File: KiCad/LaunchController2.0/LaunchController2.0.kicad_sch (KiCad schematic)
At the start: 39 parts, among them J1 CONN_ICSP, J2 CONN_USB, J3 USB_C_Receptacle_USB2.0_16P, U1 ATmega2560-16A, U2 FT232RNL, U3 USBLC6-2SC6, Y1 HUSG-16.000-20

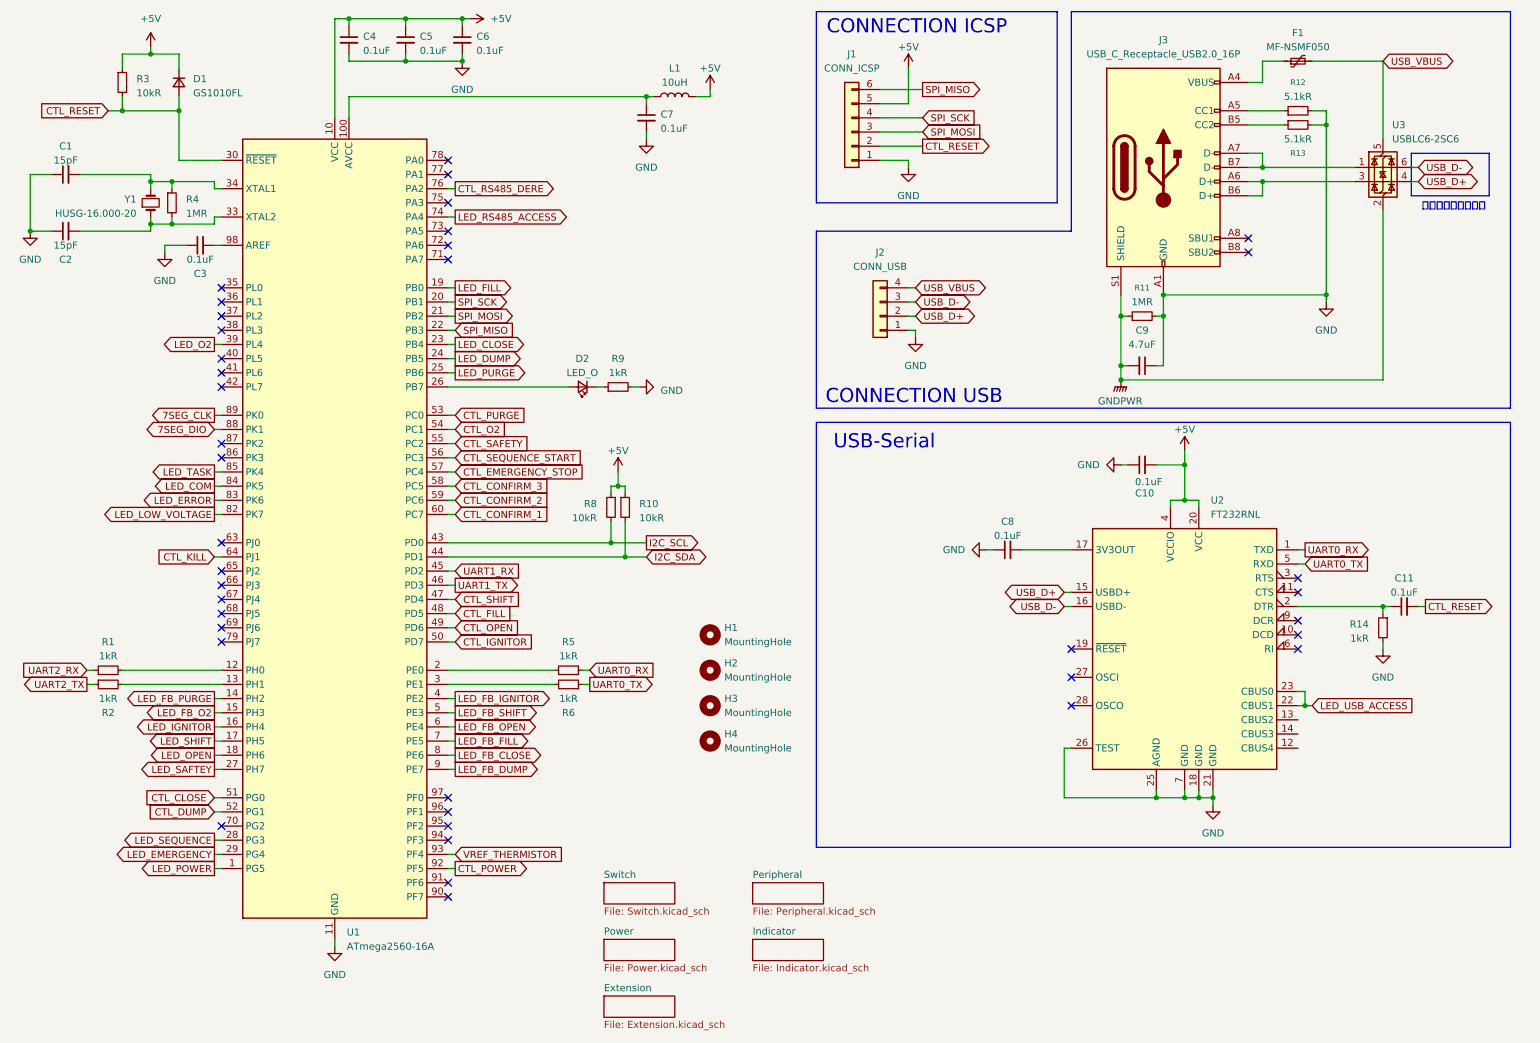
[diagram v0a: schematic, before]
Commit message: シルクなどを調整
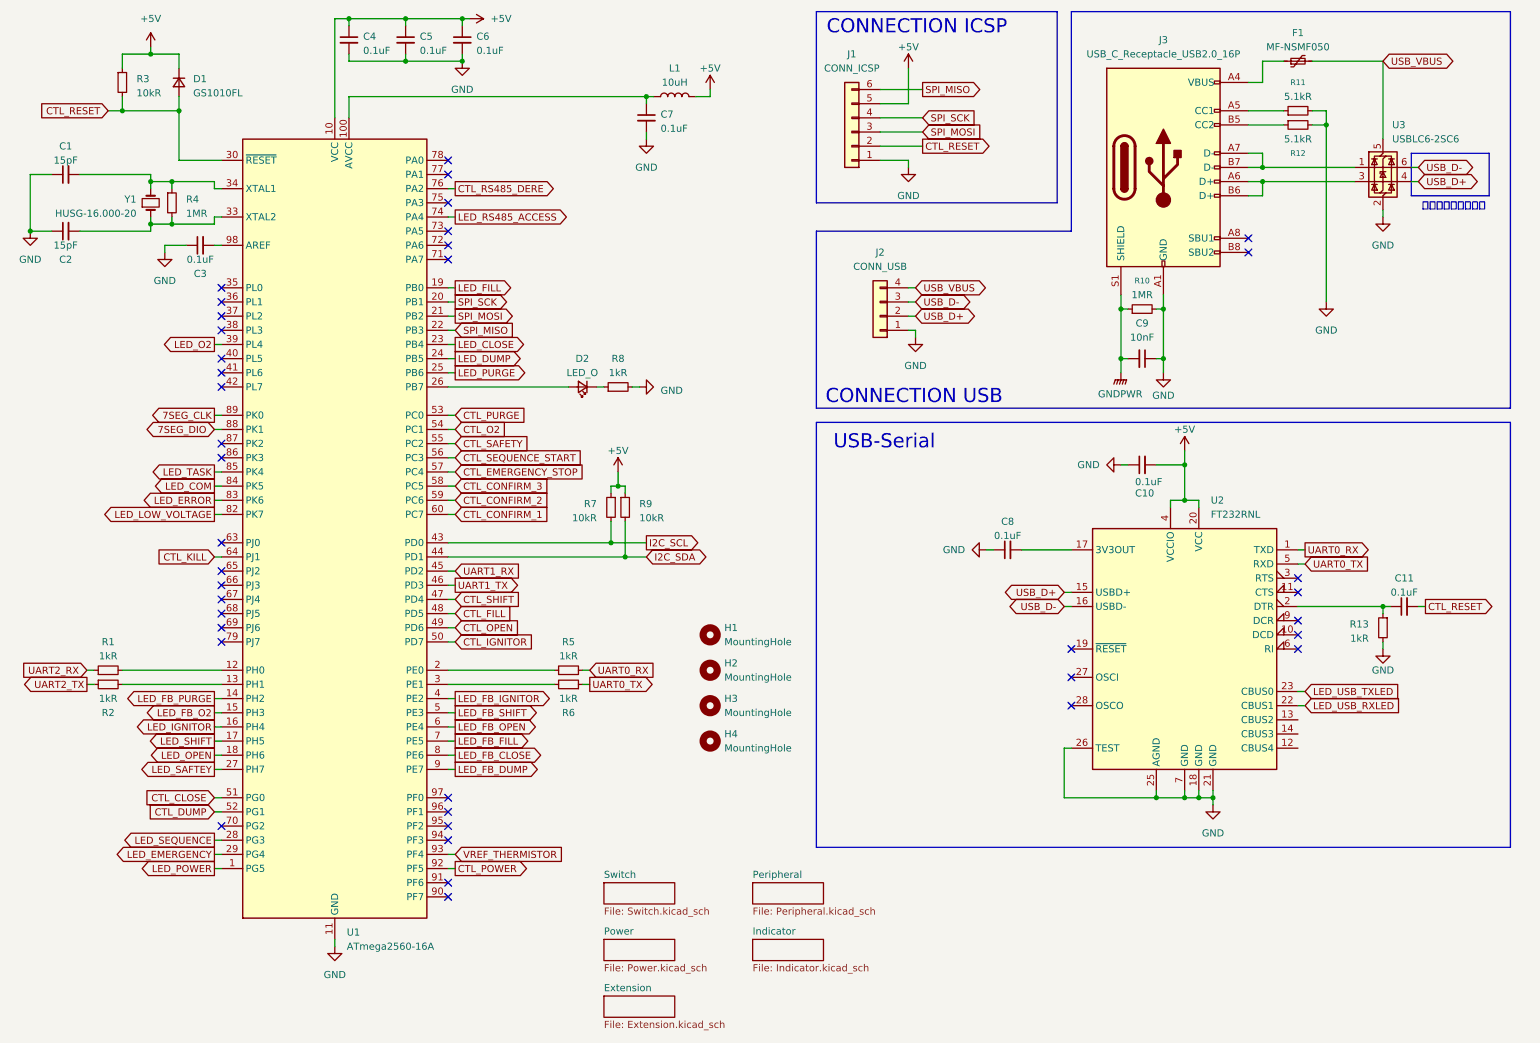
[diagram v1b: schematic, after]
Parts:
- C1, C2: Digikey_PN (none) -> 490-4941-1-ND
- C10, C11, C3, C4, C5, C6, C7, C8: Digikey_PN (none) -> 490-8020-1-ND
- C9: value 4.7uF -> 10nF; footprint Capacitor_SMD:C_0603_1608Metric_Pad1.08x0.95mm_HandSolder -> Capacitor_SMD:C_0805_2012Metric_Pad1.18x1.45mm_HandSolder; Digikey_PN (none) -> 490-GCM21B5C2E103FX0ALCT-ND
- D1: Akiduki_PN (none) -> 106014
- D2: Digikey_PN (none) -> SML-D12D8WT86CCT-ND
- F1: Akiduki_PN (none) -> 115300
- J1: Akiduki_PN (none) -> 101669
- J2: Digikey_PN (none) -> 2946-2601-3104-ND
- J3: Akiduki_PN (none) -> 114356
- L1: Akiduki_PN (none) -> 114977
- R1, R2, R5, R6: Digikey_PN (none) -> 2019-RK73H1JTTD1001FCT-ND
- R10: renamed from R11; footprint Resistor_SMD:R_0603_1608Metric_Pad0.98x0.95mm_HandSolder -> Resistor_SMD:R_1206_3216Metric_Pad1.30x1.75mm_HandSolder; Digikey_PN (none) -> 2019-RK73H2BTTD1004FCT-ND
- R11: renamed from R12; Digikey_PN (none) -> 2019-RK73H1JTTD5101FCT-ND
- R12: renamed from R13; Digikey_PN (none) -> 2019-RK73H1JTTD5101FCT-ND
- R13: renamed from R14; Digikey_PN (none) -> 2019-RK73H1JTTD1001FCT-ND
- R3: Digikey_PN (none) -> 2019-RK73H1JTTD1002FCT-ND
- R4: Digikey_PN (none) -> 2019-RK73H1JTTD1004FCT-ND
- R7: renamed from R8; Digikey_PN (none) -> 2019-RK73H1JTTD1002FCT-ND
- R8: renamed from R9; Digikey_PN (none) -> 2019-RK73H1JTTD1001FCT-ND
- R9: renamed from R10; Digikey_PN (none) -> 2019-RK73H1JTTD1002FCT-ND
- U1: Akiduki_PN (none) -> 116567
- U2: Akiduki_PN (none) -> 118243
- U3: Digikey_PN (none) -> 497-5235-1-ND
- Y1: Akiduki_PN (none) -> 108671
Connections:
- net GND: now also U3.2 (GND)
- net GNDPWR: no longer U3.2 (GND)
- net LED_USB_ACCESS renamed LED_USB_RXLED
- net LED_USB_RXLED: no longer U2.23 (CBUS0)
- new net LED_USB_TXLED: U2.23 (CBUS0)
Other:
- company: (none) -> Tokai Student Rocket Project
- moved on the sheet: C9, R10

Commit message: BOM作成
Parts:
- C1, C2: Akiduki_PN (none) -> 113312; Digikey_PN 490-4941-1-ND -> (none)
- C10, C11, C3, C4, C5, C6, C7, C8: Akiduki_PN (none) -> 114559; Digikey_PN 490-8020-1-ND -> (none)
- D2: Digikey_PN SML-D12D8WT86CCT-ND -> SML-D15DWT86CCT-ND
- H1, H2, H3, H4: footprint MountingHole:MountingHole_4mm -> MountingHole:MountingHole_4.3mm_M4_Pad_Via; now in the parts list
- U3: value USBLC6-2SC6 -> SP0504SHTG; Digikey_PN 497-5235-1-ND -> F5775CT-ND
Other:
- note added: "配線（符号）に気をつけよう"
- note removed: "向きに気をつけよう"
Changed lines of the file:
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@@
 		)
 	)
-	(text "向きに気をつけよう"
+	(text "配線（符号）に気をつけよう"
 		(exclude_from_sim no)
 		(at 270.51 49.022 0)
@@
 			)
 		)
-		(property "Datasheet" "https://www.digikey.jp/short/bbj307jp"
+		(property "Datasheet" "https://akizukidenshi.com/catalog/g/g113312/"
 			(at 21.59 53.34 0)
 			(effects
@@
 			)
 		)
-		(property "Digikey_PN" "490-4941-1-ND"
+		(property "Digikey_PN" ""
+			(at 21.59 53.34 90)
+			(effects
+				(font
+					(size 1.27 1.27)
+				)
+				(hide yes)
+			)
+		)
+		(property "Akiduki_PN" "113312"
 			(at 21.59 53.34 90)
 			(effects
@@
 			)
 		)
-		(property "Datasheet" "https://www.digikey.jp/short/ftvh328f"
+		(property "Datasheet" "https://akizukidenshi.com/catalog/g/g114559/"
 			(at 72.39 19.05 0)
 			(effects
@@
 			)
 		)
-		(property "Digikey_PN" "490-8020-1-ND"
+		(property "Digikey_PN" ""
+			(at 72.39 19.05 0)
+			(effects
+				(font
+					(size 1.27 1.27)
+				)
+				(hide yes)
+			)
+		)
+		(property "Akiduki_PN" "114559"
 			(at 72.39 19.05 0)
 			(effects
@@
 			)
 		)
-		(property "Datasheet" "https://www.digikey.jp/short/ftvh328f"
+		(property "Datasheet" "https://akizukidenshi.com/catalog/g/g114559/"
 			(at 190.5 110.49 0)
 			(effects
@@
 			)
 		)
-		(property "Digikey_PN" "490-8020-1-ND"
+		(property "Digikey_PN" ""
+			(at 190.5 110.49 90)
+			(effects
+				(font
+					(size 1.27 1.27)
+				)
+				(hide yes)
+			)
+		)
+		(property "Akiduki_PN" "114559"
 			(at 190.5 110.49 90)
 			(effects
@@
 			)
 		)
-		(property "Datasheet" "https://www.digikey.jp/short/ftvh328f"
+		(property "Datasheet" "https://akizukidenshi.com/catalog/g/g114559/"
 			(at 82.55 19.05 0)
 			(effects
@@
 			)
 		)
-		(property "Digikey_PN" "490-8020-1-ND"
+		(property "Digikey_PN" ""
+			(at 82.55 19.05 0)
+			(effects
+				(font
+					(size 1.27 1.27)
+				)
+				(hide yes)
+			)
+		)
+		(property "Akiduki_PN" "114559"
 			(at 82.55 19.05 0)
 			(effects
@@
 			)
 		)
+		(property "Mouser_PN" ""
+			(at 214.63 76.2 0)
+			(effects
+				(font
+					(size 1.27 1.27)
+				)
+				(hide yes)
+			)
+		)
+		(property "Akiduki_PN" ""
+			(at 214.63 76.2 0)
+			(effects
+				(font
+					(size 1.27 1.27)
+				)
+				(hide yes)
+			)
+		)
 		(pin "1"
 		)
@@
 			)
 		)
-		(property "Datasheet" "https://www.digikey.jp/short/ftvh328f"
+		(property "Datasheet" "https://akizukidenshi.com/catalog/g/g114559/"
 			(at 45.72 55.88 0)
 			(effects
@@
 			)
 		)
-		(property "Digikey_PN" "490-8020-1-ND"
+		(property "Digikey_PN" ""
+			(at 45.72 55.88 90)
+			(effects
+				(font
+					(size 1.27 1.27)
+				)
+				(hide yes)
+			)
+		)
+		(property "Akiduki_PN" "114559"
 			(at 45.72 55.88 90)
 			(effects
@@
 		(unit 1)
 		(exclude_from_sim no)
-		(in_bom no)
+		(in_bom yes)
 		(on_board yes)
 		(dnp no)
@@
 			)
 		)
-		(property "Footprint" "MountingHole:MountingHole_4mm"
+		(property "Footprint" "MountingHole:MountingHole_4.3mm_M4_Pad_Via"
 			(at 137.16 125.73 0)
 			(effects
@@
 			)
 		)
+		(property "Digikey_PN" ""
+			(at 137.16 125.73 0)
+			(effects
+				(font
+					(size 1.27 1.27)
+				)
+				(hide yes)
+			)
+		)
+		(property "Mouser_PN" ""
+			(at 137.16 125.73 0)
+			(effects
+				(font
+					(size 1.27 1.27)
+				)
+				(hide yes)
+			)
+		)
+		(property "Akiduki_PN" ""
+			(at 137.16 125.73 0)
+			(effects
+				(font
+					(size 1.27 1.27)
+				)
+				(hide yes)
+			)
+		)
 		(instances
 			(project ""
@@
 			)
 		)
-		(property "Value" "USBLC6-2SC6"
+		(property "Value" "SP0504SHTG"
 			(at 259.4611 36.83 0)
 			(effects
@@
 			)
 		)
-		(property "Datasheet" "https://www.digikey.jp/short/rv3q24zz"
+		(property "Datasheet" "https://www.digikey.jp/short/npv4wv57"
 			(at 259.08 50.165 0)
 			(effects
@@
 			)
 		)
-		(property "Digikey_PN" "497-5235-1-ND"
+		(property "Digikey_PN" "F5775CT-ND"
 			(at 257.81 41.91 0)
 			(effects
@@
 			)
 		)
-		(property "Datasheet" "https://www.digikey.jp/short/ftvh328f"
+		(property "Datasheet" "https://akizukidenshi.com/catalog/g/g114559/"
 			(at 261.62 120.65 0)
 			(effects
@@
 			)
 		)
-		(property "Digikey_PN" "490-8020-1-ND"
+		(property "Digikey_PN" ""
+			(at 261.62 120.65 90)
+			(effects
+				(font
+					(size 1.27 1.27)
+				)
+				(hide yes)
+			)
+		)
+		(property "Akiduki_PN" "114559"
 			(at 261.62 120.65 90)
 			(effects
@@
 			)
 		)
-		(property "Datasheet" "https://www.digikey.jp/short/ftvh328f"
+		(property "Datasheet" "https://akizukidenshi.com/catalog/g/g114559/"
 			(at 214.63 95.25 0)
 			(effects
@@
 			)
 		)
-		(property "Digikey_PN" "490-8020-1-ND"
+		(property "Digikey_PN" ""
+			(at 214.63 95.25 90)
+			(effects
+				(font
+					(size 1.27 1.27)
+				)
+				(hide yes)
+			)
+		)
+		(property "Akiduki_PN" "114559"
 			(at 214.63 95.25 90)
 			(effects
@@
 		(unit 1)
 		(exclude_from_sim no)
-		(in_bom no)
+		(in_bom yes)
 		(on_board yes)
 		(dnp no)
@@
 			)
 		)
-		(property "Footprint" "MountingHole:MountingHole_4mm"
+		(property "Footprint" "MountingHole:MountingHole_4.3mm_M4_Pad_Via"
 			(at 137.16 132.08 0)
 			(effects
@@
 			)
 		)
-		(property "Datasheet" "https://www.digikey.jp/short/ftvh328f"
+		(property "Datasheet" "https://akizukidenshi.com/catalog/g/g114559/"
 			(at 125.73 33.02 0)
 			(effects
@@
 			)
 		)
-		(property "Digikey_PN" "490-8020-1-ND"
+		(property "Digikey_PN" ""
+			(at 125.73 33.02 0)
+			(effects
+				(font
+					(size 1.27 1.27)
+				)
+				(hide yes)
+			)
+		)
+		(property "Akiduki_PN" "114559"
 			(at 125.73 33.02 0)
 			(effects
@@
 		(unit 1)
 		(exclude_from_sim no)
-		(in_bom no)
+		(in_bom yes)
 		(on_board yes)
 		(dnp no)
@@
 			)
 		)
-		(property "Footprint" "MountingHole:MountingHole_4mm"
+		(property "Footprint" "MountingHole:MountingHole_4.3mm_M4_Pad_Via"
 			(at 137.16 138.43 0)
 			(effects
@@
 			)
 		)
+		(property "Digikey_PN" ""
+			(at 218.44 41.91 0)
+			(effects
+				(font
+					(size 1.27 1.27)
+				)
+				(hide yes)
+			)
+		)
+		(property "Mouser_PN" ""
+			(at 218.44 41.91 0)
+			(effects
+				(font
+					(size 1.27 1.27)
+				)
+				(hide yes)
+			)
+		)
 		(pin "A1"
 		)
@@
 			)
 		)
-		(property "Datasheet" "https://www.digikey.jp/short/ftvh328f"
+		(property "Datasheet" "https://akizukidenshi.com/catalog/g/g114559/"
 			(at 92.71 19.05 0)
 			(effects
@@
 			)
 		)
-		(property "Digikey_PN" "490-8020-1-ND"
+		(property "Digikey_PN" ""
+			(at 92.71 19.05 0)
+			(effects
+				(font
+					(size 1.27 1.27)
+				)
+				(hide yes)
+			)
+		)
+		(property "Akiduki_PN" "114559"
 			(at 92.71 19.05 0)
 			(effects
@@
 		(unit 1)
 		(exclude_from_sim no)
-		(in_bom no)
+		(in_bom yes)
 		(on_board yes)
 		(dnp no)
@@
 			)
 		)
-		(property "Footprint" "MountingHole:MountingHole_4mm"
+		(property "Footprint" "MountingHole:MountingHole_4.3mm_M4_Pad_Via"
 			(at 137.16 144.78 0)
 			(effects
@@
 			)
 		)
-		(property "Datasheet" "https://www.digikey.jp/short/3p7j3w3t"
+		(property "Datasheet" "https://www.digikey.jp/short/3ww5zf50"
 			(at 114.3 81.28 90)
 			(effects
@@
 			)
 		)
-		(property "Digikey_PN" "SML-D12D8WT86CCT-ND"
+		(property "Digikey_PN" "SML-D15DWT86CCT-ND"
 			(at 114.3 81.28 0)
 			(effects
@@
 			)
 		)
-		(property "Datasheet" "https://www.digikey.jp/short/bbj307jp"
+		(property "Datasheet" "https://akizukidenshi.com/catalog/g/g113312/"
 			(at 21.59 43.18 0)
 			(effects
@@
 			)
 		)
-		(property "Digikey_PN" "490-4941-1-ND"
+		(property "Digikey_PN" ""
+			(at 21.59 43.18 90)
+			(effects
+				(font
+					(size 1.27 1.27)
+				)
+				(hide yes)
+			)
+		)
+		(property "Akiduki_PN" "113312"
 			(at 21.59 43.18 90)
 			(effects

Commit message: とりあえずプッシュ
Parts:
- C9: DigiKey_PN (none) -> 490-GCM21B5C2E103FX0ALCT-ND
- D2: DigiKey_PN (none) -> 160-1434-1-ND
- J2: DigiKey_PN (none) -> 2946-2601-3104-ND
- R1, R13, R2, R5, R6, R8: DigiKey_PN (none) -> 2019-RK73H1JTTD1001FCT-ND
- R10: DigiKey_PN (none) -> 2019-RK73H2BTTD1004FCT-ND
- R11, R12: DigiKey_PN (none) -> 2019-RK73H1JTTD5101FCT-ND
- R3, R7, R9: DigiKey_PN (none) -> 2019-RK73H1JTTD1002FCT-ND
- R4: DigiKey_PN (none) -> 2019-RK73H1JTTD1004FCT-ND
- U3: value SP0504SHTG -> USBLC6-2SC6Y; DigiKey_PN (none) -> 497-11882-1-ND; Digikey_PN F5775CT-ND -> 497-11882-1-ND
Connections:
- no-connect marks 39 -> 42
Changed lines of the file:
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@@
 	)
 	(no_connect
+		(at 242.57 140.97)
+	)
+	(no_connect
 		(at 49.53 109.22)
 	)
@@
 	)
 	(no_connect
+		(at 242.57 143.51)
+	)
+	(no_connect
 		(at 49.53 63.5)
 	)
@@
 	)
 	(no_connect
+		(at 242.57 146.05)
+	)
+	(no_connect
 		(at 49.53 93.98)
 	)
@@
 			)
 		)
+		(property "DigiKey_PN" "2019-RK73H1JTTD1001FCT-ND"
+			(at 29.21 134.62 90)
+			(effects
+				(font
+					(size 1.27 1.27)
+				)
+				(hide yes)
+			)
+		)
 		(pin "1"
 		)
@@
 			)
 		)
+		(property "DigiKey_PN" "2019-RK73H1JTTD1004FCT-ND"
+			(at 40.64 48.26 0)
+			(effects
+				(font
+					(size 1.27 1.27)
+				)
+				(hide yes)
+			)
+		)
 		(pin "1"
 		)
@@
 			)
 		)
+		(property "DigiKey_PN" "2019-RK73H1JTTD5101FCT-ND"
+			(at 242.57 31.75 90)
+			(effects
+				(font
+					(size 1.27 1.27)
+				)
+				(hide yes)
+			)
+		)
 		(pin "2"
 		)
@@
 			)
 		)
+		(property "DigiKey_PN" "490-GCM21B5C2E103FX0ALCT-ND"
+			(at 214.63 76.2 90)
+			(effects
+				(font
+					(size 1.27 1.27)
+				)
+				(hide yes)
+			)
+		)
 		(pin "1"
 		)
@@
 			)
 		)
+		(property "DigiKey_PN" "2019-RK73H1JTTD1002FCT-ND"
+			(at 31.75 26.67 0)
+			(effects
+				(font
+					(size 1.27 1.27)
+				)
+				(hide yes)
+			)
+		)
 		(pin "1"
 		)
@@
 			)
 		)
-		(property "Value" "SP0504SHTG"
+		(property "Value" "USBLC6-2SC6Y"
 			(at 259.4611 36.83 0)
 			(effects
@@
 			)
 		)
-		(property "Datasheet" "https://www.digikey.jp/short/npv4wv57"
+		(property "Datasheet" "https://www.digikey.jp/short/tjz00fwn"
 			(at 259.08 50.165 0)
 			(effects
@@
 			)
 		)
-		(property "Digikey_PN" "F5775CT-ND"
+		(property "Digikey_PN" "497-11882-1-ND"
+			(at 257.81 41.91 0)
+			(effects
+				(font
+					(size 1.27 1.27)
+				)
+				(hide yes)
+			)
+		)
+		(property "DigiKey_PN" "497-11882-1-ND"
 			(at 257.81 41.91 0)
 			(effects
@@
 			)
 		)
+		(property "DigiKey_PN" "2019-RK73H1JTTD1001FCT-ND"
+			(at 111.76 134.62 90)
+			(effects
+				(font
+					(size 1.27 1.27)
+				)
+				(hide yes)
+			)
+		)
 		(pin "1"
 		)
@@
 			)
 		)
+		(property "DigiKey_PN" "2019-RK73H1JTTD1001FCT-ND"
+			(at 111.76 132.08 90)
+			(effects
+				(font
+					(size 1.27 1.27)
+				)
+				(hide yes)
+			)
+		)
 		(pin "1"
 		)
@@
 			)
 		)
+		(property "DigiKey_PN" "2019-RK73H1JTTD1001FCT-ND"
+			(at 257.81 124.46 0)
+			(effects
+				(font
+					(size 1.27 1.27)
+				)
+				(hide yes)
+			)
+		)
 		(pin "1"
 		)
@@
 			)
 		)
+		(property "DigiKey_PN" "2019-RK73H1JTTD1002FCT-ND"
+			(at 119.38 102.87 0)
+			(effects
+				(font
+					(size 1.27 1.27)
+				)
+				(hide yes)
+			)
+		)
 		(pin "1"
 		)
@@
 			)
 		)
+		(property "DigiKey_PN" "2019-RK73H2BTTD1004FCT-ND"
+			(at 214.63 67.31 90)
+			(effects
+				(font
+					(size 1.27 1.27)
+				)
+				(hide yes)
+			)
+		)
 		(pin "1"
 		)
@@
 			)
 		)
+		(property "DigiKey_PN" "2019-RK73H1JTTD1001FCT-ND"
+			(at 29.21 132.08 90)
+			(effects
+				(font
+					(size 1.27 1.27)
+				)
+				(hide yes)
+			)
+		)
 		(pin "1"
 		)
@@
 			)
 		)
+		(property "DigiKey_PN" "2019-RK73H1JTTD1002FCT-ND"
+			(at 121.92 102.87 0)
+			(effects
+				(font
+					(size 1.27 1.27)
+				)
+				(hide yes)
+			)
+		)
 		(pin "1"
 		)
@@
 			)
 		)
+		(property "DigiKey_PN" "2019-RK73H1JTTD1001FCT-ND"
+			(at 120.65 81.28 90)
+			(effects
+				(font
+					(size 1.27 1.27)
+				)
+				(hide yes)
+			)
+		)
 		(pin "1"
 		)
@@
 			)
 		)
+		(property "DigiKey_PN" "2946-2601-3104-ND"
+			(at 167.64 68.58 0)
+			(effects
+				(font
+					(size 1.27 1.27)
+				)
+				(hide yes)
+			)
+		)
 		(pin "1"
 		)
@@
 			)
 		)
-		(property "Datasheet" "https://www.digikey.jp/short/3ww5zf50"
+		(property "Datasheet" "https://www.digikey.jp/short/58tn8j9t"
 			(at 114.3 81.28 90)
 			(effects
@@
 			)
 		)
+		(property "DigiKey_PN" "160-1434-1-ND"
+			(at 114.3 81.28 0)
+			(effects
+				(font
+					(size 1.27 1.27)
+				)
+				(hide yes)
+			)
+		)
 		(pin "1"
 		)
@@
 			(at 242.57 34.29 90)
 			(effects
+				(font
+					(size 1.27 1.27)
+				)
+				(hide yes)
+			)
+		)
+		(property "DigiKey_PN" "2019-RK73H1JTTD5101FCT-ND"
+			(at 242.57 34.29 90)
+			(effects
